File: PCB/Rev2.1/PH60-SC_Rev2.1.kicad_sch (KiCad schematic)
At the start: 48 parts, among them J1 USB_C_Receptacle_USB2.0_14P, J2 Conn_01x02_Pin, J3 Conn_01x02_Pin, U1 nRF52840, U5 LIS2DE12, X1 32.768kHz, X2 Crystal_Generic

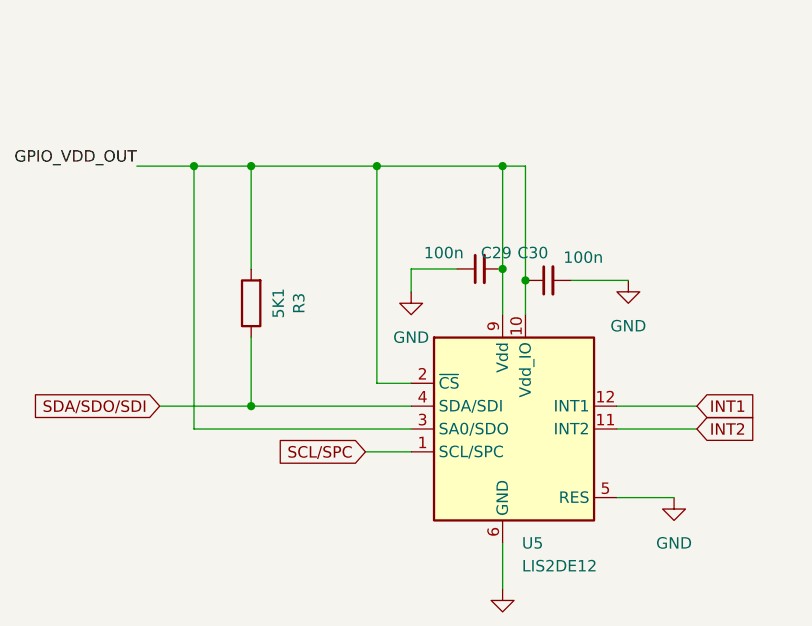
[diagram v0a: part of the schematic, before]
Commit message: 为imu的scl添加5.1kΩ上拉电阻并调整pcb布局
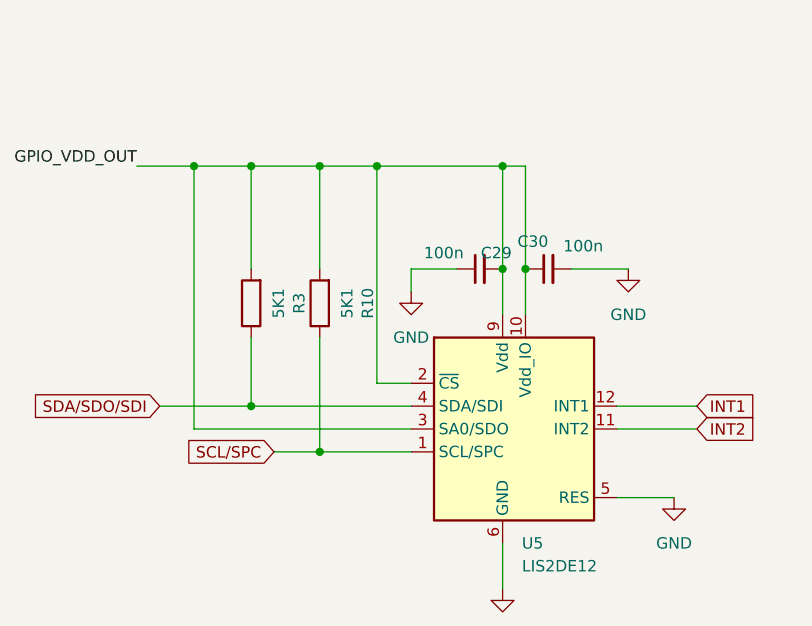
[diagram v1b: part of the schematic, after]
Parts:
- added R10: 5K1, Resistor_SMD:R_0402_1005Metric, symbol Device:R
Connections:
- net GPIO_VDD_OUT: now also R10.2
- net SCL/SPC: now also R10.1
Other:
- moved on the sheet: C30
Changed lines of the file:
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@@
 	)
 	(junction
-		(at 127 189.23)
-		(diameter 0)
-		(color 0 0 0 0)
-	)
-	(junction
 		(at 52.07 43.18)
 		(diameter 0)
@@
 	)
 	(junction
+		(at 104.14 208.28)
+		(diameter 0)
+		(color 0 0 0 0)
+	)
+	(junction
+		(at 127 187.96)
+		(diameter 0)
+		(color 0 0 0 0)
+	)
+	(junction
 		(at 124.46 187.96)
 		(diameter 0)
@@
 		(color 0 0 0 0)
 	)
+	(junction
+		(at 104.14 176.53)
+		(diameter 0)
+		(color 0 0 0 0)
+	)
 	(no_connect
 		(at 241.3 101.6)
@@
 	(wire
 		(pts
-			(xy 109.22 208.28) (xy 114.3 208.28)
+			(xy 99.06 208.28) (xy 104.14 208.28)
 		)
 		(stroke
@@
 	(wire
 		(pts
+			(xy 104.14 208.28) (xy 114.3 208.28)
+		)
+		(stroke
+			(width 0)
+			(type default)
+		)
+	)
+	(wire
+		(pts
 			(xy 166.37 162.56) (xy 175.26 162.56)
 		)
@@
 	(wire
 		(pts
-			(xy 127 176.53) (xy 127 189.23)
+			(xy 127 176.53) (xy 127 187.96)
 		)
 		(stroke
@@
 	(wire
 		(pts
-			(xy 96.52 176.53) (xy 110.49 176.53)
+			(xy 96.52 176.53) (xy 104.14 176.53)
 		)
 		(stroke
@@
 	(wire
 		(pts
-			(xy 138.43 189.23) (xy 132.08 189.23)
+			(xy 138.43 187.96) (xy 132.08 187.96)
 		)
 		(stroke
@@
 	(wire
 		(pts
+			(xy 104.14 195.58) (xy 104.14 208.28)
+		)
+		(stroke
+			(width 0)
+			(type default)
+		)
+	)
+	(wire
+		(pts
 			(xy 49.53 27.94) (xy 57.15 27.94)
 		)
@@
 	(wire
 		(pts
+			(xy 104.14 176.53) (xy 104.14 187.96)
+		)
+		(stroke
+			(width 0)
+			(type default)
+		)
+	)
+	(wire
+		(pts
 			(xy 43.18 147.32) (xy 52.07 147.32)
 		)
@@
 	(wire
 		(pts
+			(xy 104.14 176.53) (xy 110.49 176.53)
+		)
+		(stroke
+			(width 0)
+			(type default)
+		)
+	)
+	(wire
+		(pts
 			(xy 208.28 190.5) (xy 208.28 195.58)
 		)
@@
 	(wire
 		(pts
-			(xy 127 189.23) (xy 127 193.04)
-		)
-		(stroke
-			(width 0)
-			(type default)
-		)
-	)
-	(wire
-		(pts
 			(xy 67.31 35.56) (xy 67.31 38.1)
 		)
@@
 	(wire
 		(pts
+			(xy 127 187.96) (xy 127 193.04)
+		)
+		(stroke
+			(width 0)
+			(type default)
+		)
+	)
+	(wire
+		(pts
 			(xy 34.29 66.04) (xy 34.29 67.31)
 		)
@@
 	(global_label "SCL{slash}SPC"
 		(shape input)
-		(at 109.22 208.28 180)
+		(at 99.06 208.28 180)
 		(fields_autoplaced yes)
 		(effects
@@
 		)
 		(property "Intersheetrefs" "${INTERSHEET_REFS}"
-			(at 97.6472 208.28 0)
+			(at 87.4872 208.28 0)
 			(hide yes)
 			(show_name no)
@@
 	)
 	(symbol
+		(lib_id "Device:R")
+		(at 104.14 191.77 180)
+		(unit 1)
+		(body_style 1)
+		(exclude_from_sim no)
+		(in_bom yes)
+		(on_board yes)
+		(in_pos_files yes)
+		(dnp no)
+		(property "Reference" "R10"
+			(at 109.474 191.77 90)
+			(show_name no)
+			(do_not_autoplace no)
+			(effects
+				(font
+					(size 1.27 1.27)
+				)
+			)
+		)
+		(property "Value" "5K1"
+			(at 107.188 191.77 90)
+			(show_name no)
+			(do_not_autoplace no)
+			(effects
+				(font
+					(size 1.27 1.27)
+				)
+			)
+		)
+		(property "Footprint" "Resistor_SMD:R_0402_1005Metric"
+			(at 105.918 191.77 90)
+			(hide yes)
+			(show_name no)
+			(do_not_autoplace no)
+			(effects
+				(font
+					(size 1.27 1.27)
+				)
+			)
+		)
+		(property "Datasheet" ""
+			(at 104.14 191.77 0)
+			(hide yes)
+			(show_name no)
+			(do_not_autoplace no)
+			(effects
+				(font
+					(size 1.27 1.27)
+				)
+			)
+		)
+		(property "Description" "Resistor"
+			(at 104.14 191.77 0)
+			(hide yes)
+			(show_name no)
+			(do_not_autoplace no)
+			(effects
+				(font
+					(size 1.27 1.27)
+				)
+			)
+		)
+		(pin "1"
+		)
+		(pin "2"
+		)
+		(instances
+			(project "PH60-SC_Rev2.1"
+				(path "/dca0f898-8fdb-4522-a51d-f4f4238906e7"
+					(reference "R10")
+					(unit 1)
+				)
+			)
+		)
+	)
+	(symbol
 		(lib_id "Device:L_Small")
 		(at 283.21 30.48 0)
@@
 	(symbol
 		(lib_id "Device:C_Small")
-		(at 129.54 189.23 90)
+		(at 129.54 187.96 90)
 		(unit 1)
 		(body_style 1)
@@
 		(dnp no)
 		(property "Reference" "C30"
-			(at 129.54 186.182 90)
+			(at 129.54 184.912 90)
 			(show_name no)
 			(do_not_autoplace no)
@@
 		)
 		(property "Value" "100n"
-			(at 135.636 186.69 90)
+			(at 135.636 185.42 90)
 			(show_name no)
 			(do_not_autoplace no)
@@
 		)
 		(property "Footprint" "Capacitor_SMD:C_0402_1005Metric"
-			(at 129.54 189.23 0)
+			(at 129.54 187.96 0)
 			(hide yes)
 			(show_name no)
@@
 		)
 		(property "Datasheet" ""
-			(at 129.54 189.23 0)
+			(at 129.54 187.96 0)
 			(hide yes)
 			(show_name no)
@@
 		)
 		(property "Description" "Unpolarized capacitor, small symbol"
-			(at 129.54 189.23 0)
+			(at 129.54 187.96 0)
 			(hide yes)
 			(show_name no)
@@
 	(symbol
 		(lib_id "power:GND")
-		(at 138.43 189.23 0)
+		(at 138.43 187.96 0)
 		(unit 1)
 		(body_style 1)
@@
 		(fields_autoplaced yes)
 		(property "Reference" "#PWR023"
-			(at 138.43 195.58 0)
+			(at 138.43 194.31 0)
 			(hide yes)
 			(show_name no)
@@
 		)
 		(property "Value" "GND"
-			(at 138.43 194.31 0)
+			(at 138.43 193.04 0)
 			(show_name no)
 			(do_not_autoplace no)
@@
 		)
 		(property "Footprint" ""
-			(at 138.43 189.23 0)
+			(at 138.43 187.96 0)
 			(hide yes)
 			(show_name no)
@@
 		)
 		(property "Datasheet" ""
-			(at 138.43 189.23 0)
+			(at 138.43 187.96 0)
 			(hide yes)
 			(show_name no)
@@
 		)
 		(property "Description" "Power symbol creates a global label with name \"GND\" , ground"
-			(at 138.43 189.23 0)
+			(at 138.43 187.96 0)
 			(hide yes)
 			(show_name no)

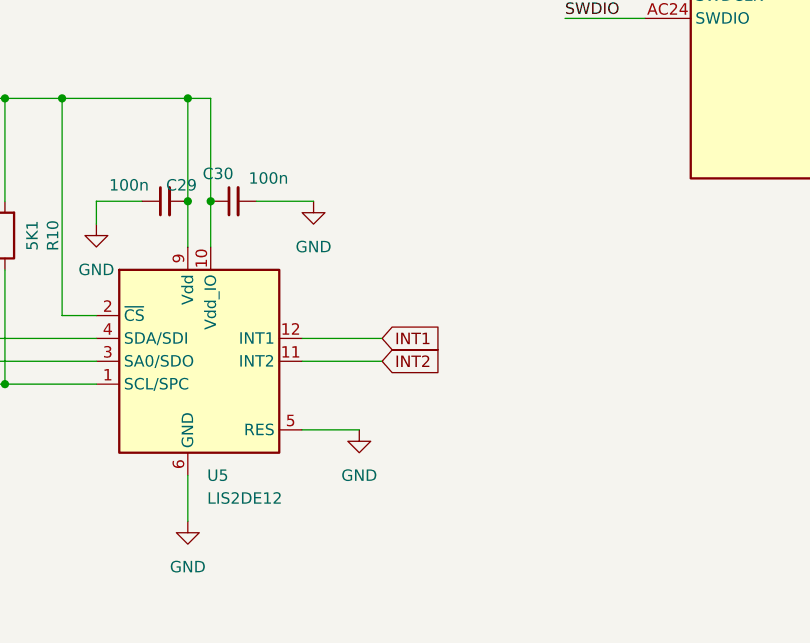
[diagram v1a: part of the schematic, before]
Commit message: 为LIS2DE12的INT1/INT2引脚添加1MΩ下拉电阻
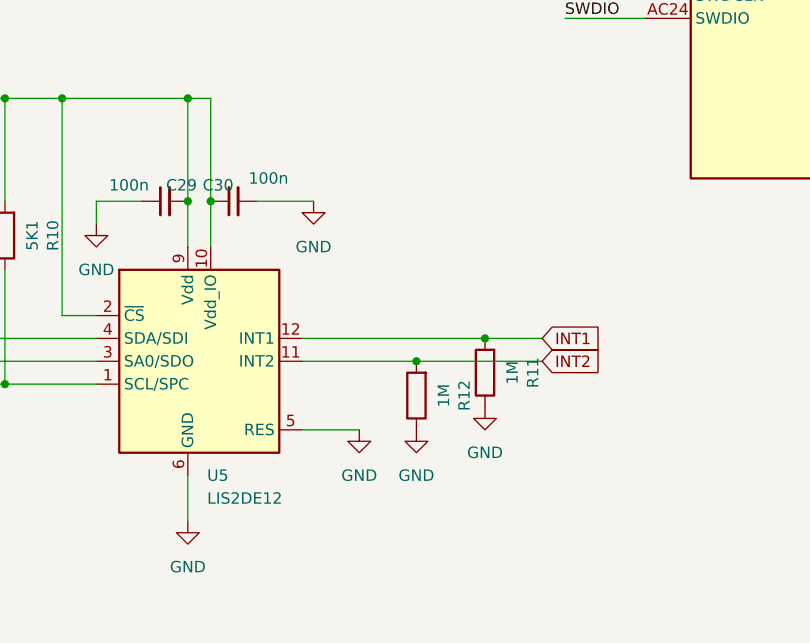
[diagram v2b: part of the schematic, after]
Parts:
- added R11, R12: 1M, Resistor_SMD:R_0402_1005Metric, symbol Device:R
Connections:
- net GND: now also R11.1, R12.1
- net INT1: now also R11.2
- net INT2: now also R12.2

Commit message: 调整imu滤波电容
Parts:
- removed C29: 100n, Capacitor_SMD:C_0402_1005Metric, symbol Device:C_Small
- C30: value 100n -> 10u
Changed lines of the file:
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@@
 	)
 	(junction
-		(at 124.46 187.96)
-		(diameter 0)
-		(color 0 0 0 0)
-	)
-	(junction
 		(at 283.21 34.29)
 		(diameter 0)
@@
 	(wire
 		(pts
-			(xy 124.46 187.96) (xy 124.46 193.04)
-		)
-		(stroke
-			(width 0)
-			(type default)
-		)
-	)
-	(wire
-		(pts
 			(xy 143.51 114.3) (xy 143.51 118.11)
 		)
@@
 	(wire
 		(pts
-			(xy 114.3 187.96) (xy 114.3 190.5)
-		)
-		(stroke
-			(width 0)
-			(type default)
-		)
-	)
-	(wire
-		(pts
 			(xy 149.86 20.32) (xy 149.86 21.59)
 		)
@@
 	(wire
 		(pts
-			(xy 124.46 176.53) (xy 124.46 187.96)
+			(xy 124.46 176.53) (xy 124.46 193.04)
 		)
 		(stroke
@@
 	(wire
 		(pts
-			(xy 119.38 187.96) (xy 114.3 187.96)
-		)
-		(stroke
-			(width 0)
-			(type default)
-		)
-	)
-	(wire
-		(pts
 			(xy 52.07 40.64) (xy 52.07 43.18)
 		)
@@
 			)
 		)
-		(property "Value" "100n"
+		(property "Value" "10u"
 			(at 135.636 185.42 90)
 			(show_name no)
@@
 	)
 	(symbol
-		(lib_id "Device:C_Small")
-		(at 121.92 187.96 90)
-		(unit 1)
-		(body_style 1)
-		(exclude_from_sim no)
-		(in_bom yes)
-		(on_board yes)
-		(in_pos_files yes)
-		(dnp no)
-		(property "Reference" "C29"
-			(at 125.476 186.182 90)
-			(show_name no)
-			(do_not_autoplace no)
-			(effects
-				(font
-					(size 1.27 1.27)
-				)
-				(justify left)
-			)
-		)
-		(property "Value" "100n"
-			(at 120.142 186.182 90)
-			(show_name no)
-			(do_not_autoplace no)
-			(effects
-				(font
-					(size 1.27 1.27)
-				)
-				(justify left)
-			)
-		)
-		(property "Footprint" "Capacitor_SMD:C_0402_1005Metric"
-			(at 121.92 187.96 0)
-			(hide yes)
-			(show_name no)
-			(do_not_autoplace no)
-			(effects
-				(font
-					(size 1.27 1.27)
-				)
-			)
-		)
-		(property "Datasheet" ""
-			(at 121.92 187.96 0)
-			(hide yes)
-			(show_name no)
-			(do_not_autoplace no)
-			(effects
-				(font
-					(size 1.27 1.27)
-				)
-			)
-		)
-		(property "Description" "Unpolarized capacitor, small symbol"
-			(at 121.92 187.96 0)
-			(hide yes)
-			(show_name no)
-			(do_not_autoplace no)
-			(effects
-				(font
-					(size 1.27 1.27)
-				)
-			)
-		)
-		(pin "2"
-		)
-		(pin "1"
-		)
-		(instances
-			(project "PH60-SC_Rev2.1"
-				(path "/dca0f898-8fdb-4522-a51d-f4f4238906e7"
-					(reference "C29")
-					(unit 1)
-				)
-			)
-		)
-	)
-	(symbol
 		(lib_id "Device:R")
 		(at 245.11 180.34 90)
@@
 					(unit 1)
 				)
-			)
-		)
-	)
-	(symbol
-		(lib_id "power:GND")
-		(at 114.3 190.5 0)
-		(unit 1)
-		(body_style 1)
-		(exclude_from_sim no)
-		(in_bom yes)
-		(on_board yes)
-		(in_pos_files yes)
-		(dnp no)
-		(fields_autoplaced yes)
-		(property "Reference" "#PWR036"
-			(at 114.3 196.85 0)
-			(hide yes)
-			(show_name no)
-			(do_not_autoplace no)
-			(effects
-				(font
-					(size 1.27 1.27)
-				)
-			)
-		)
-		(property "Value" "GND"
-			(at 114.3 195.58 0)
-			(show_name no)
-			(do_not_autoplace no)
-			(effects
-				(font
-					(size 1.27 1.27)
-				)
-			)
-		)
-		(property "Footprint" ""
-			(at 114.3 190.5 0)
-			(hide yes)
-			(show_name no)
-			(do_not_autoplace no)
-			(effects
-				(font
-					(size 1.27 1.27)
-				)
-			)
-		)
-		(property "Datasheet" ""
-			(at 114.3 190.5 0)
-			(hide yes)
-			(show_name no)
-			(do_not_autoplace no)
-			(effects
-				(font
-					(size 1.27 1.27)
-				)
-			)
-		)
-		(property "Description" "Power symbol creates a global label with name \"GND\" , ground"
-			(at 114.3 190.5 0)
-			(hide yes)
-			(show_name no)
-			(do_not_autoplace no)
-			(effects
-				(font
-					(size 1.27 1.27)
-				)
-			)
-		)
-		(pin "1"
-		)
-		(instances
-			(project "PH60-SC_Rev2.1"
-				(path "/dca0f898-8fdb-4522-a51d-f4f4238906e7"
-					(reference "#PWR036")
-					(unit 1)
-				)

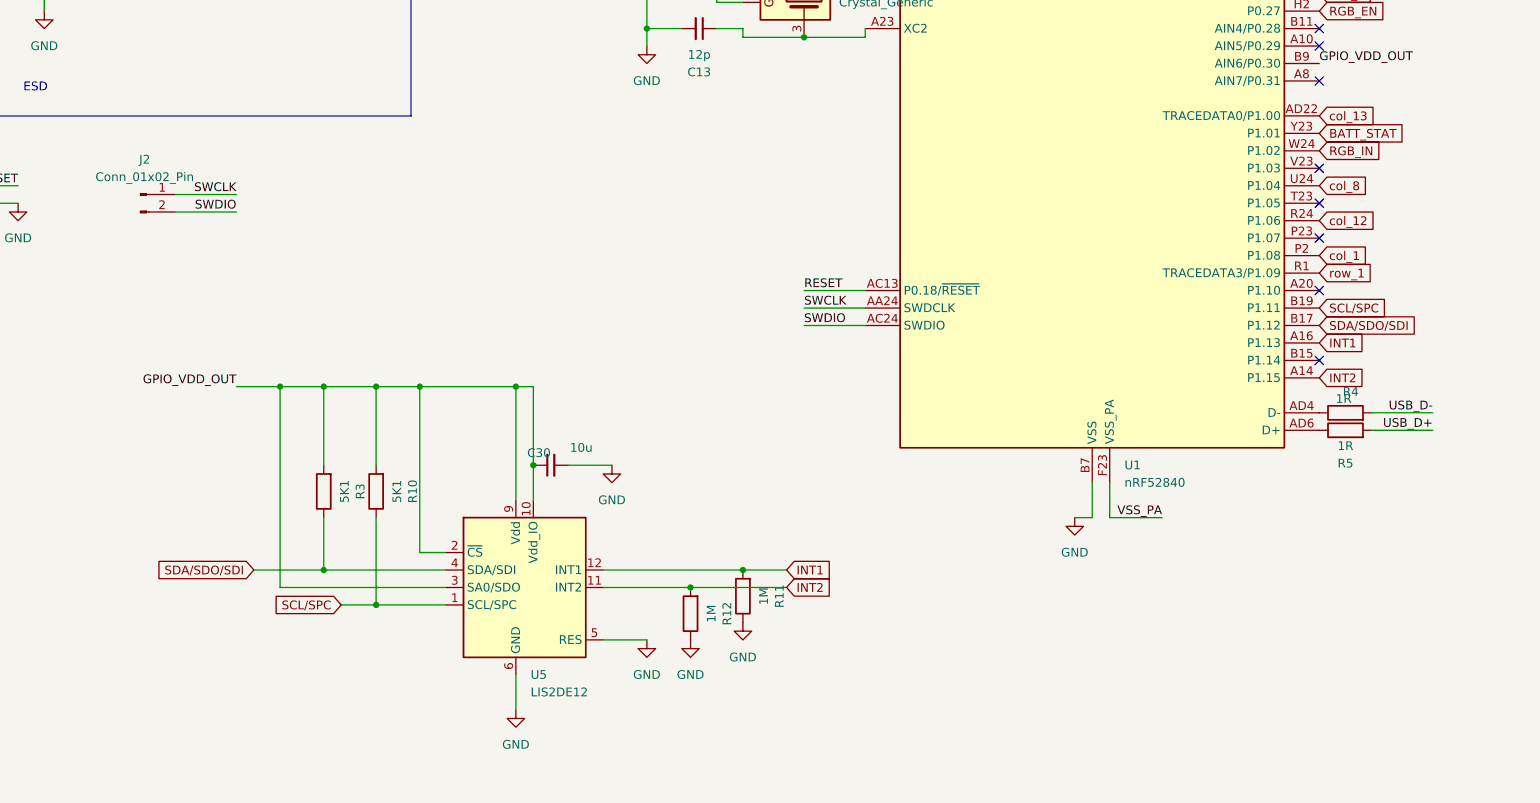
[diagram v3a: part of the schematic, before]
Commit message: Delete resistor and route
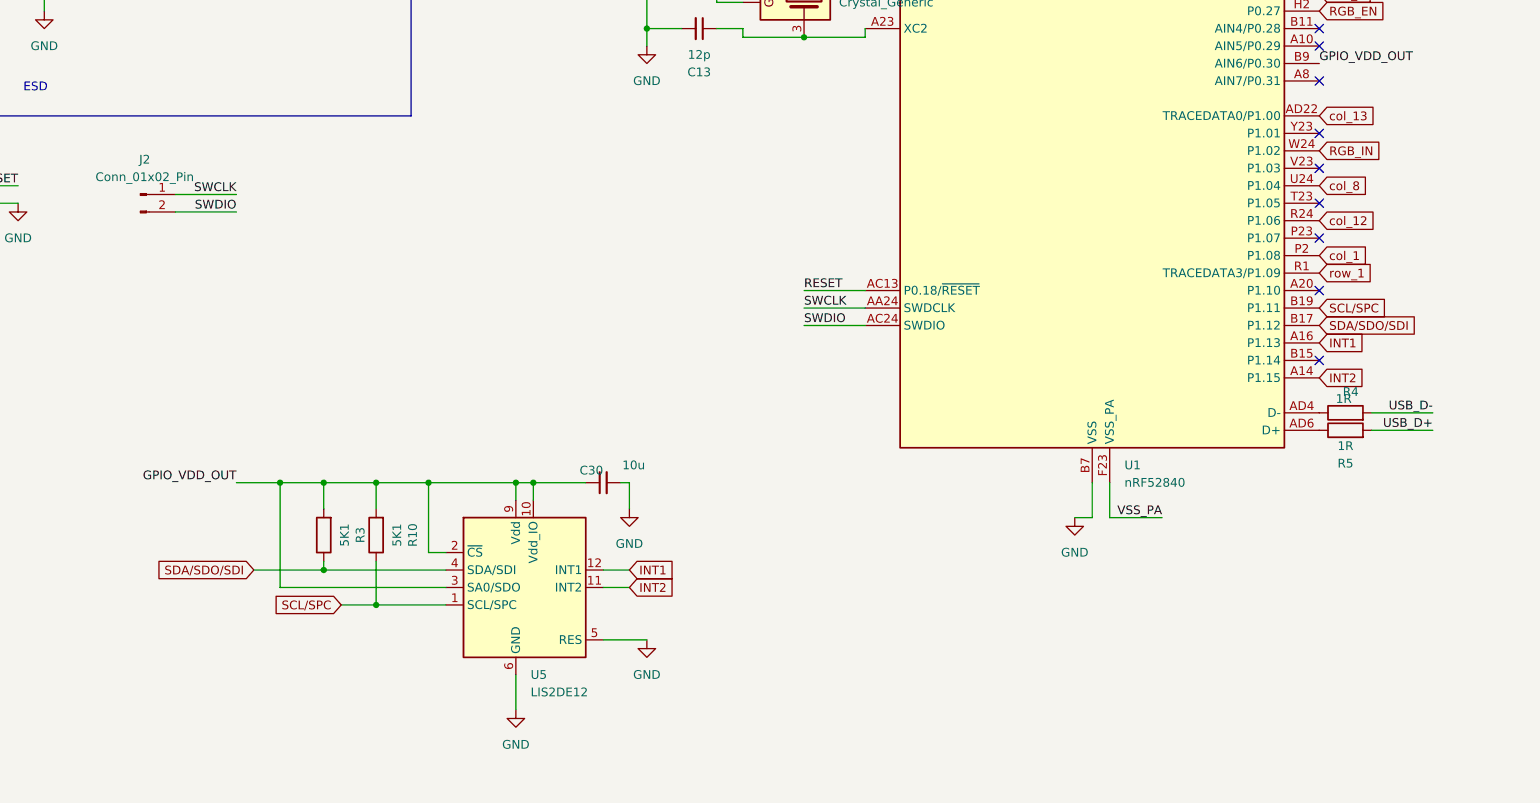
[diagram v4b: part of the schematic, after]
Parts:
- removed R11, R12: 1M, Resistor_SMD:R_0402_1005Metric, symbol Device:R
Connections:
- net BATT_STAT: no longer names the net of U1.Y23 (P1.01)
- no-connect marks 19 -> 20
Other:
- moved on the sheet: C30, R10, R3

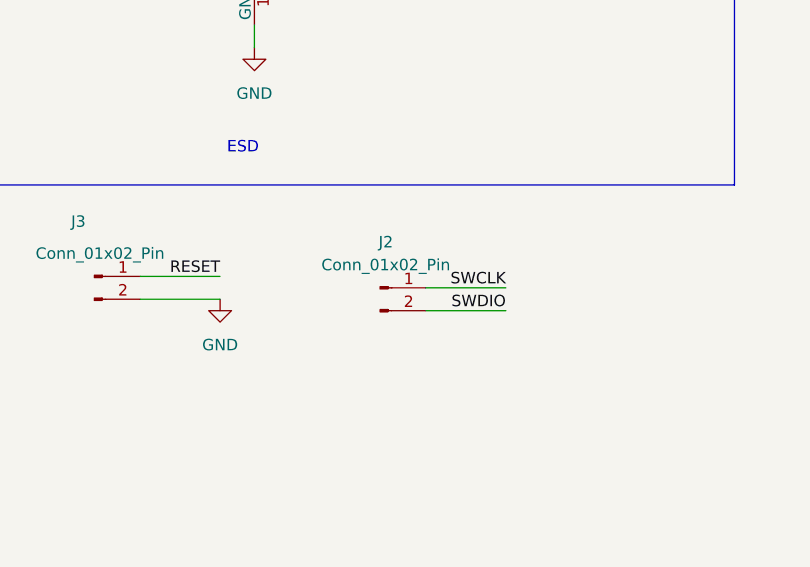
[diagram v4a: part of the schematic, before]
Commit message: 修改烧录口5 线烧录接法（SWD 模式），pin  1.27mm
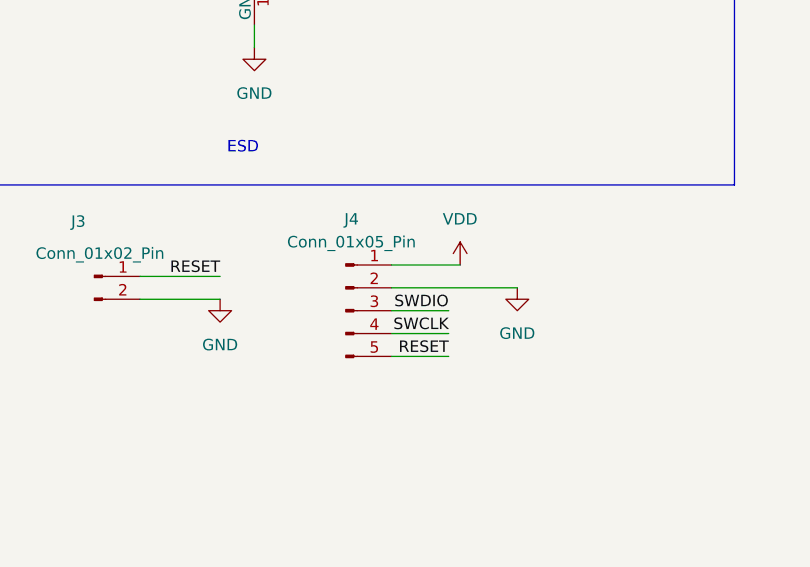
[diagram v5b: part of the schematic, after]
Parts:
- removed J2: Conn_01x02_Pin, Connector_PinHeader_2.00mm:PinHeader_1x02_P2.00mm_Vertical, symbol Connector:Conn_01x02_Pin
- added J4: Conn_01x05_Pin, Connector_PinHeader_1.27mm:PinHeader_1x05_P1.27mm_Vertical, symbol Connector:Conn_01x05_Pin
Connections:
- net GND: now also J4.2 (Pin_2)
- net RESET: now also J4.5 (Pin_5)
- net SWCLK: now also J4.4 (Pin_4)
- net SWDIO: now also J4.3 (Pin_3)
- net VDD: now also J4.1 (Pin_1)
